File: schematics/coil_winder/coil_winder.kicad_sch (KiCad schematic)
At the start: 11 parts, among them J1 Stepper_Motor_1, J2 Stepper_Motor_2, J3 Barrel_Jack, SW1 RotaryEncoder_Switch, U1 Pico, U2 L7805

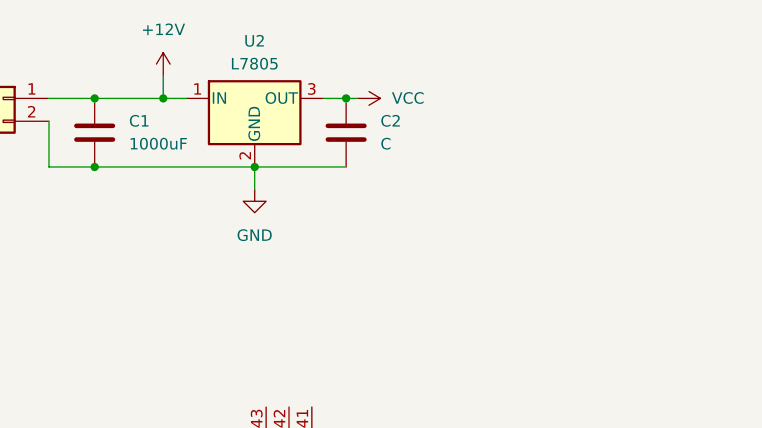
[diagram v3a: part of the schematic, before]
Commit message: Specify cap val
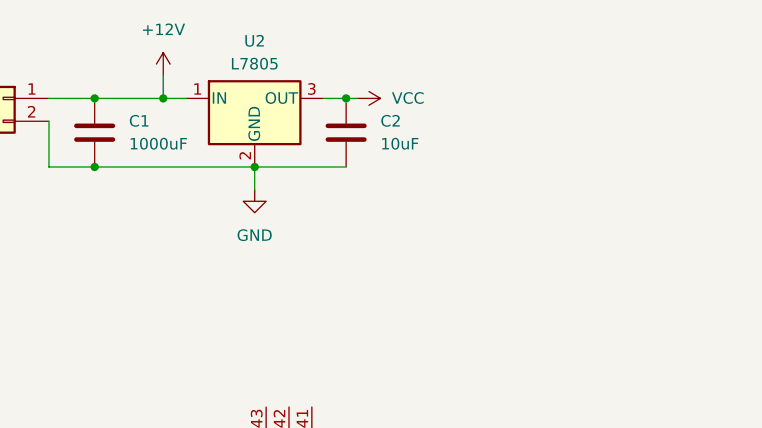
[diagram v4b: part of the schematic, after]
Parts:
- C2: value C -> 10uF
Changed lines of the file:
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@@
       (effects (font (size 1.27 1.27)) (justify left))
     )
-    (property "Value" "C" (at 175.26 29.21 0)
+    (property "Value" "10uF" (at 175.26 29.21 0)
       (effects (font (size 1.27 1.27)) (justify left))
     )

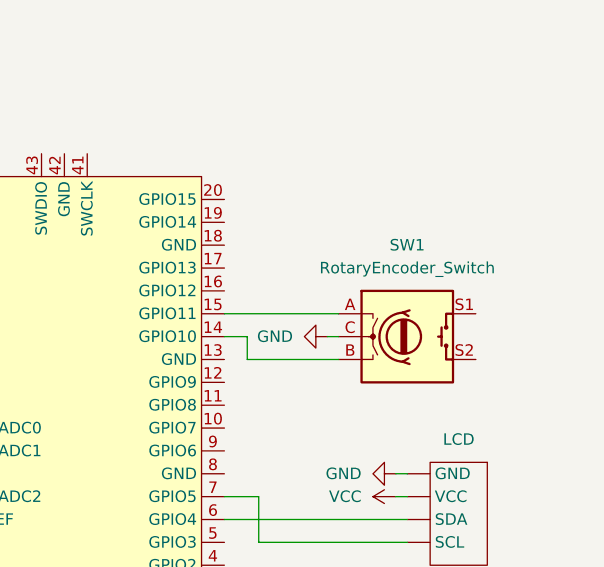
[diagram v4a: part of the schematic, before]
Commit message: Hook up encoder pushbutton
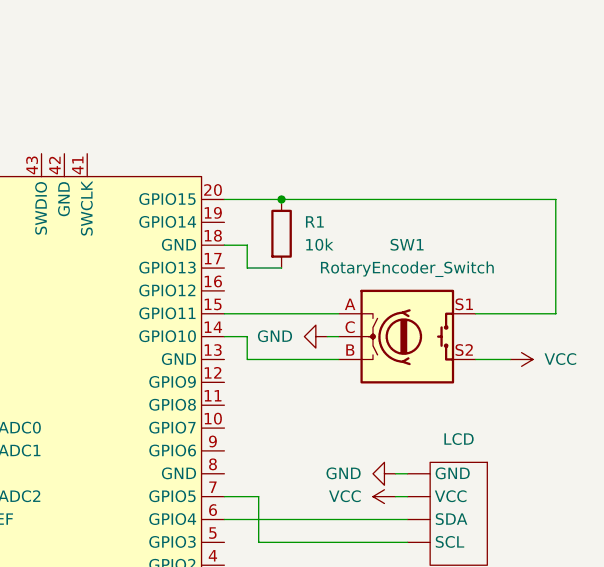
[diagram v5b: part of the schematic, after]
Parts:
- added R1: 10k, symbol Device:R
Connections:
- net VCC: now also SW1.S2
- net at U1.18 (GND): now also R1.2
- net at U1.20 (GPIO15): now also SW1.S1, R1.1
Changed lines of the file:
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@@
   (junction (at 143.51 31.75) (diameter 0) (color 0 0 0 0)
   )
+  (junction (at 189.23 63.5) (diameter 0) (color 0 0 0 0)
+  )
   (junction (at 85.09 82.55) (diameter 0) (color 0 0 0 0)
   )
@@
     (stroke (width 0) (type default))
   )
+  (wire (pts (xy 189.23 63.5) (xy 182.88 63.5))
+    (stroke (width 0) (type default))
+  )
   (wire (pts (xy 186.69 96.52) (xy 182.88 96.52))
     (stroke (width 0) (type default))
@@
     (stroke (width 0) (type default))
   )
+  (wire (pts (xy 210.82 81.28) (xy 214.63 81.28))
+    (stroke (width 0) (type default))
+  )
   (wire (pts (xy 90.17 80.01) (xy 90.17 82.55))
     (stroke (width 0) (type default))
@@
     (stroke (width 0) (type default))
   )
+  (wire (pts (xy 185.42 71.12) (xy 185.42 68.58))
+    (stroke (width 0) (type default))
+  )
   (wire (pts (xy 138.43 26.67) (xy 138.43 31.75))
     (stroke (width 0) (type default))
@@
     (stroke (width 0) (type default))
   )
+  (wire (pts (xy 219.71 63.5) (xy 189.23 63.5))
+    (stroke (width 0) (type default))
+  )
   (wire (pts (xy 97.79 128.27) (xy 101.6 128.27))
     (stroke (width 0) (type default))
@@
     (stroke (width 0) (type default))
   )
+  (wire (pts (xy 210.82 76.2) (xy 219.71 76.2))
+    (stroke (width 0) (type default))
+  )
+  (wire (pts (xy 185.42 68.58) (xy 182.88 68.58))
+    (stroke (width 0) (type default))
+  )
+  (wire (pts (xy 219.71 76.2) (xy 219.71 63.5))
+    (stroke (width 0) (type default))
+  )
   (wire (pts (xy 74.93 113.03) (xy 72.39 113.03))
+    (stroke (width 0) (type default))
+  )
+  (wire (pts (xy 189.23 71.12) (xy 185.42 71.12))
     (stroke (width 0) (type default))
   )
@@
     )
   )
+  (symbol (lib_id "power:VCC") (at 214.63 81.28 270) (unit 1)
+    (in_bom yes) (on_board yes) (dnp no) (fields_autoplaced)
+    (property "Reference" "#PWR017" (at 210.82 81.28 0)
+      (effects (font (size 1.27 1.27)) hide)
+    )
+    (property "Value" "VCC" (at 218.44 81.28 90)
+      (effects (font (size 1.27 1.27)) (justify left))
+    )
+    (property "Footprint" "" (at 214.63 81.28 0)
+      (effects (font (size 1.27 1.27)) hide)
+    )
+    (property "Datasheet" "" (at 214.63 81.28 0)
+      (effects (font (size 1.27 1.27)) hide)
+    )
+    (pin "1")
+    (instances
+      (project "coil_winder"
+        (path "/5ec64e02-ee9b-4809-b355-36a61de13204"
+          (reference "#PWR017") (unit 1)
+        )
+      )
+    )
+  )
   (symbol (lib_id "Device:RotaryEncoder_Switch") (at 203.2 78.74 0) (unit 1)
     (in_bom yes) (on_board yes) (dnp no)
@@
         )
       )
+    )
+  )
+  (symbol (lib_id "Device:R") (at 189.23 67.31 0) (unit 1)
+    (in_bom yes) (on_board yes) (dnp no) (fields_autoplaced)
+    (property "Reference" "R1" (at 191.77 66.04 0)
+      (effects (font (size 1.27 1.27)) (justify left))
+    )
+    (property "Value" "10k" (at 191.77 68.58 0)
+      (effects (font (size 1.27 1.27)) (justify left))
+    )
+    (property "Footprint" "" (at 187.452 67.31 90)
+      (effects (font (size 1.27 1.27)) hide)
+    )
+    (property "Datasheet" "~" (at 189.23 67.31 0)
+      (effects (font (size 1.27 1.27)) hide)
+    )
+    (pin "1")
+    (pin "2")
+    (instances
+      (project "coil_winder"
+        (path "/5ec64e02-ee9b-4809-b355-36a61de13204"
+          (reference "R1") (unit 1)
+        )
+      )
